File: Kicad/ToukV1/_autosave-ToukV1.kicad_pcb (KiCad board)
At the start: 2 copper layers, 5 parts, among them J1 M1_T, J2 M2_T

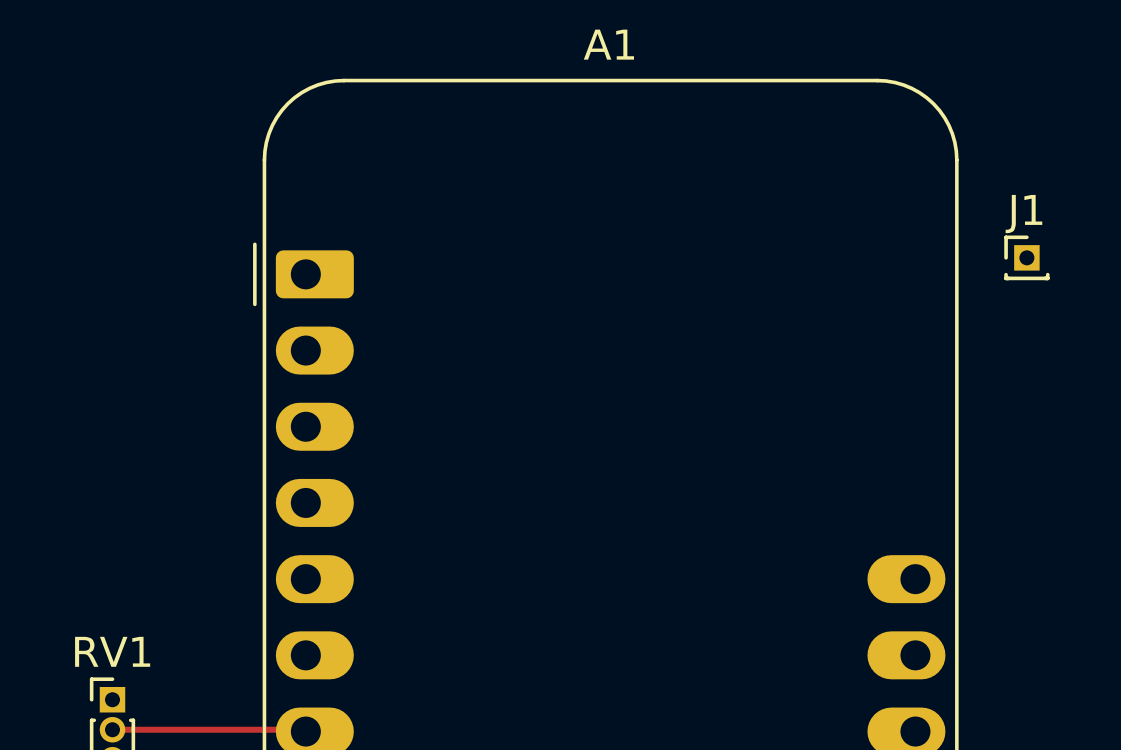
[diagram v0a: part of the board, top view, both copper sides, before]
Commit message: Ajout des Faders au Kicad
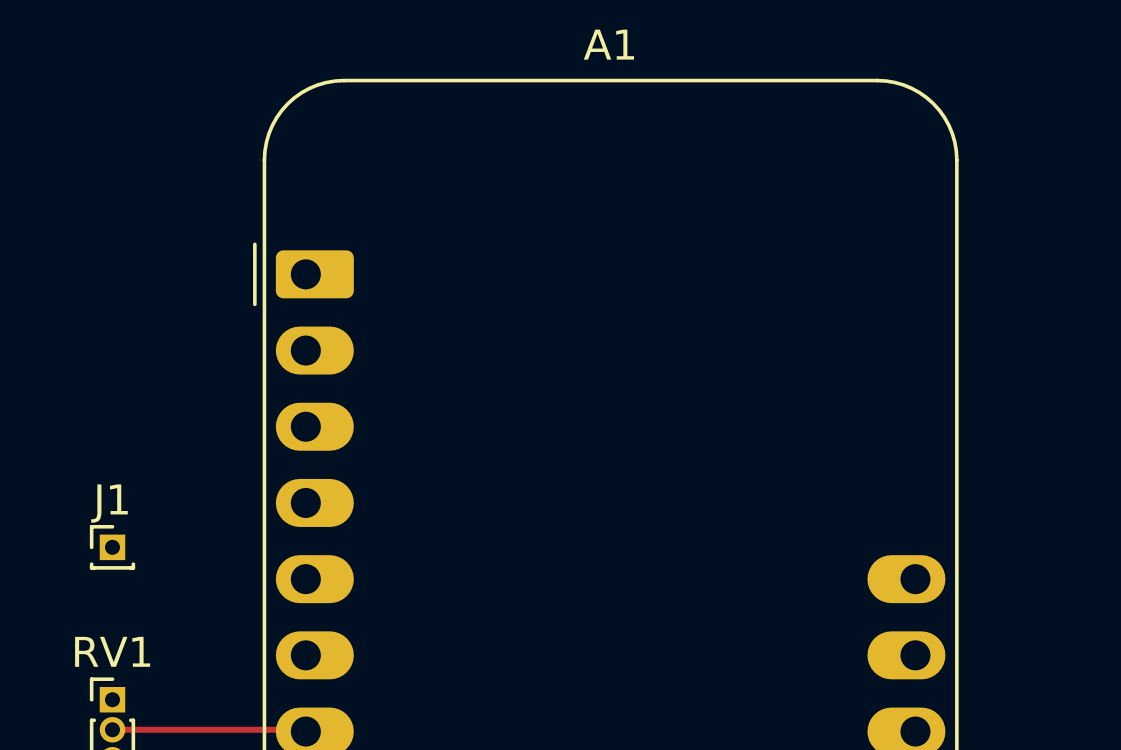
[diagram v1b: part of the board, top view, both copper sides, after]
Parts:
- moved J1 32.0 mm to (73.7, 50.8)
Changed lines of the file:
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@@
   (net 30 "T1")
   (footprint "Connector_PinHeader_1.00mm:PinHeader_1x01_P1.00mm_Vertical" (layer "F.Cu")
-    (at 104.14 41.15)
+    (at 73.66 50.8)
     (descr "Through hole straight pin header, 1x01, 1.00mm pitch, single row")
     (tags "Through hole pin header THT 1x01 1.00mm single row")
